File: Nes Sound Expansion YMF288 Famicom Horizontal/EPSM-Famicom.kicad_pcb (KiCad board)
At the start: 4 copper layers, 99 x 91.7 mm, 60 parts, among them J1 CARTRIDGE_F, J2 OUT_1, J3 EPSM_ADDRESSING, J4 CONSOLE_M, J5 AudioJack4_SwitchTR1, U1 74LS174, U10 74LS257, U2 74LS174, U3 74LS139, U4 74LS132, U5 YMF288, U6 BU9480F, U7 74LS257, U8 74LS257, U9 LM358, X1 SG-8002CA

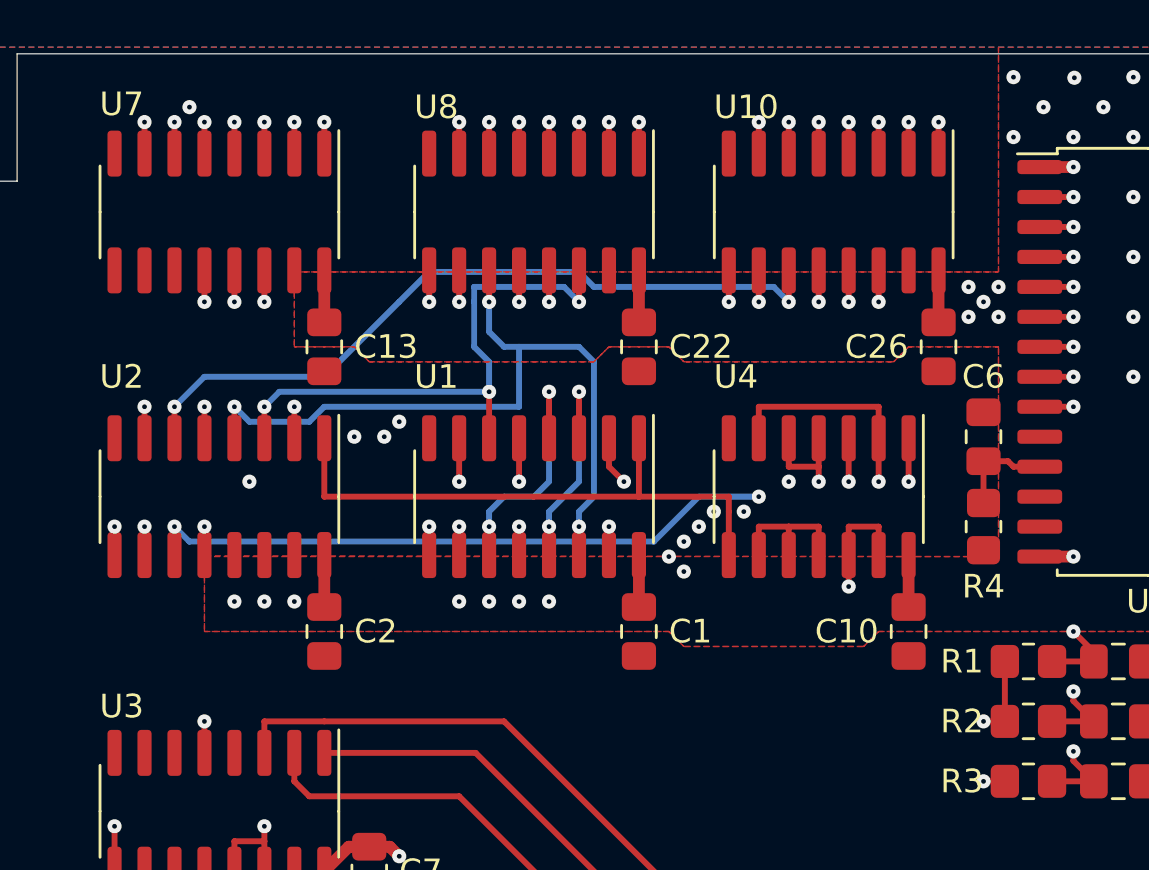
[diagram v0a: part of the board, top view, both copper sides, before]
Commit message: Fix erroneous $4016 data latch lines
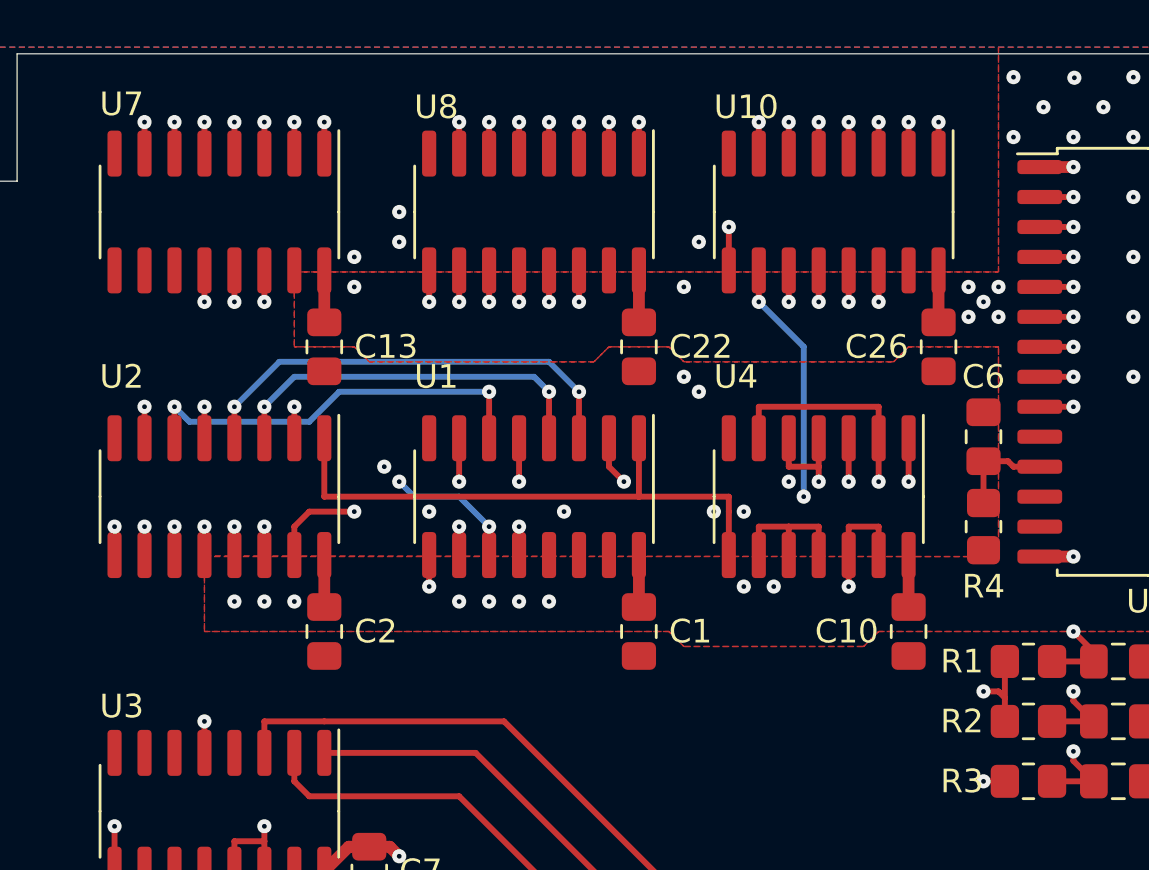
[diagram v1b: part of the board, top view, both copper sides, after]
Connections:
- U1 pad 10: /BUF_D5 -> /BUF_D3
- U1 pad 11: /CPU_D5 -> /CPU_D7
- U1 pad 12: /BUF_D4 -> /$4016_EN
- U1 pad 13: /CPU_D4 -> /VCC
- U1 pad 14: /CPU_D7 -> unconnected-(U1-Pad14)
- U1 pad 15: /BUF_D3 -> unconnected-(U1-Pad15)
- U2 pad 10: /BUF_A1 -> /BUF_D7
- U2 pad 11: /CPU_D2 -> /CPU_D7
- U2 pad 12: /$4016_EN -> /BUF_A0
- U2 pad 13: /VCC -> /CPU_D3
- U2 pad 14: /VCC -> /CPU_D2
- U2 pad 15: unconnected-(U2-Pad15) -> /BUF_A1
- U2 pad 2: /BUF_D6 -> /BUF_D5
- U2 pad 3: /CPU_D6 -> /CPU_D5
- U2 pad 4: /CPU_D7 -> /CPU_D4
- U2 pad 5: /BUF_D7 -> /BUF_D4
- U2 pad 6: /CPU_D3 -> /CPU_D6
- U2 pad 7: /BUF_A0 -> /BUF_D6
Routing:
- net /BUF_D6: track 15.8 -> 31.4 mm
- net /BUF_D3: track 16.9 -> 27.2 mm
- net /CPU_D4: track 104.8 -> 113.2 mm, vias 4 -> 5
- net /BUF_A0: track 27.0 -> 35.0 mm, vias 3 -> 4
- net /CPU_D6: track 104.3 -> 110.7 mm
- net /$4016_EN: track 86.2 -> 80.1 mm, vias 6 -> 5
- net /BUF_CS: track 37.0 -> 31.1 mm, vias 3 -> 2
- net /CPU_D3: track 110.5 -> 104.7 mm, vias 2 -> 3
- net /BUF_A1: track 20.2 -> 25.4 mm, vias 2 -> 3
- net /BUF_D7: track 17.8 -> 22.1 mm
- net /YM_D3: track 19.2 -> 22.9 mm
- net /BUF_D5: track 22.8 -> 19.3 mm
- net /BUF_D4: track 29.9 -> 26.7 mm, vias 3 -> 2
- net /CPU_D7: track 102.4 -> 99.1 mm, vias 3 -> 4
- net /CPU_D2: track 108.3 -> 105.1 mm
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
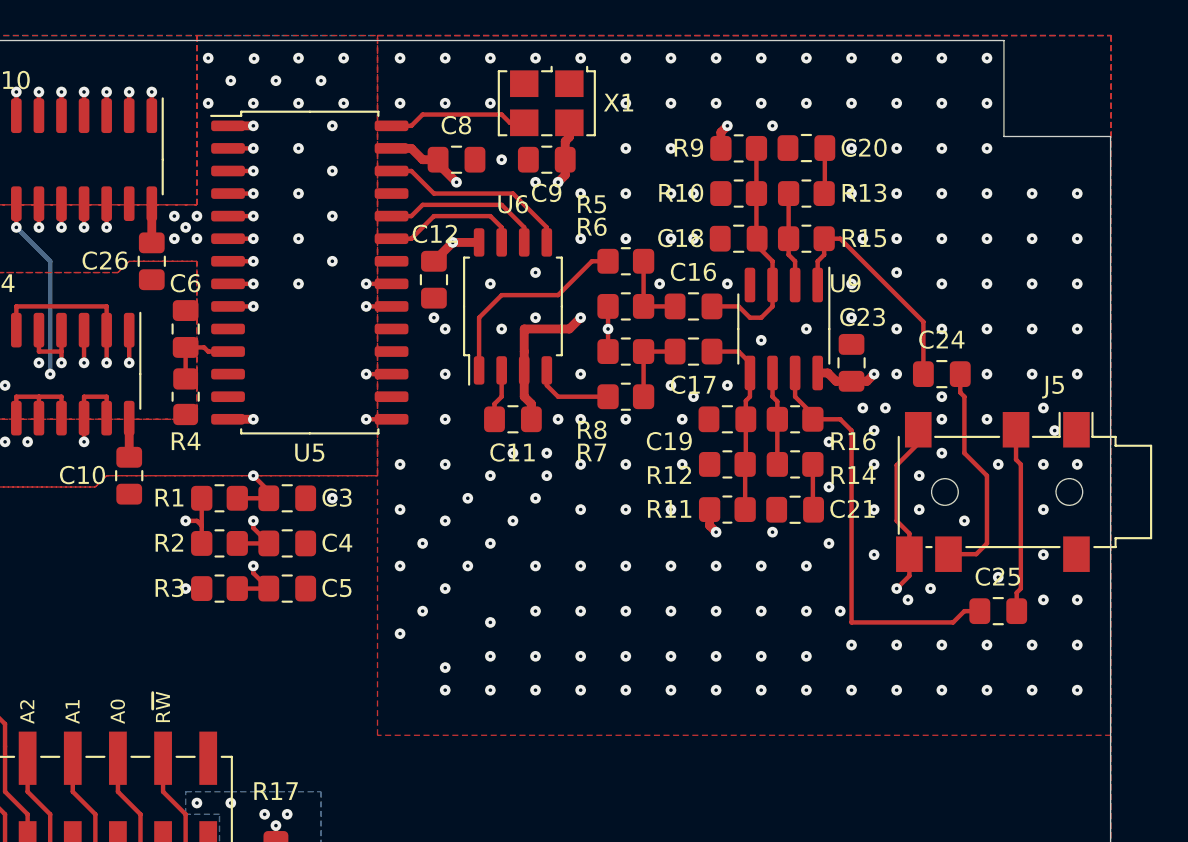
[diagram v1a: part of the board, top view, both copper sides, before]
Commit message: Fix footprint size errors
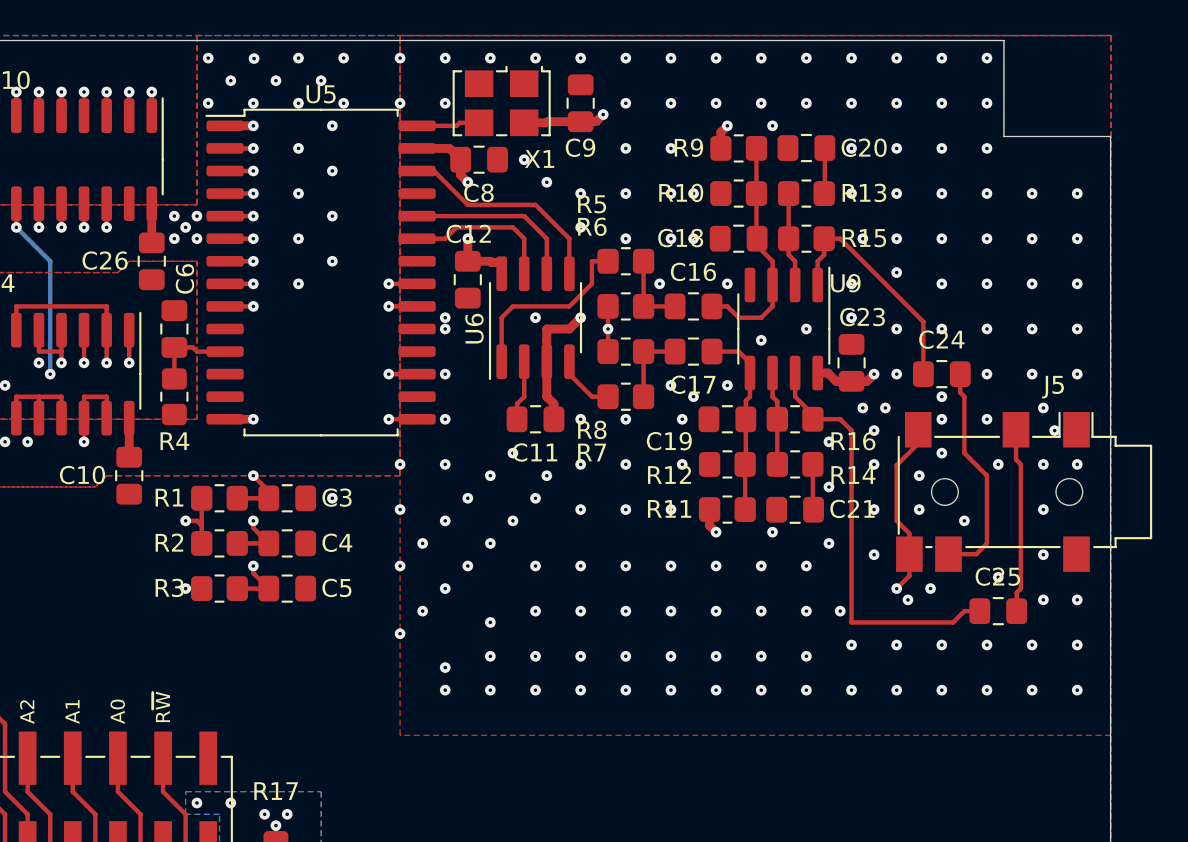
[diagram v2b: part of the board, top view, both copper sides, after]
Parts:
- U1, U2: value 74LS174 -> 74HC174
- U10, U7, U8: value 74LS257 -> 74HC257
- U3: value 74LS139 -> 74HC139
- U4: value 74LS132 -> 74HC132
- U5: footprint EPSM-Famicom:SOP-28_7.5x12.8mm_P1.27mm -> EPSM-Famicom:SOP-28_8.4x18.1mm_P1.27mm
- U6: footprint Package_SO:SOIC-8_5.275x5.275mm_P1.27mm -> Package_SO:SOIC-8_3.9x4.9mm_P1.27mm
- moved C9 3.70 mm to (146.7, 49.5), turned to 90 degrees
- moved X1 2.54 mm to (142.2, 49.5)
- moved C12 1.91 mm to (140.3, 59.5)
- moved U6 1.42 mm to (144.1, 61.6)
- moved C11 1.27 mm to (144.1, 67.3)
- moved C8 1.27 mm to (141.0, 52.7)
- moved U5 0.64 mm to (132.1, 59.1)
- moved C6 0.63 mm to (123.8, 62.2)
- moved R4 0.63 mm to (123.8, 66.0)
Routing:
- net Net-(U5-Pad28): track 7.92 -> 3.56 mm
- net Net-(U5-Pad26): track 10.9 -> 12.9 mm
- net Net-(R5-Pad2): track 11.5 -> 9.88 mm
- net /VCC: track 37.1 -> 38.7 mm
- net Net-(U5-Pad23): track 7.83 -> 9.33 mm
- net Net-(U5-Pad24): track 9.10 -> 10.6 mm
- net /YM_CS: track 49.9 -> 51.2 mm
- net /YM_A1: track 52.2 -> 53.5 mm
- net /YM_A0: track 54.5 -> 55.8 mm
- net /GND: track 52.2 -> 50.9 mm, vias 244 -> 237
- net /AUD_RF: track 57.9 -> 57.2 mm
- net /~{IRQ}: track 71.9 -> 72.4 mm
- net Net-(R7-Pad2): track 4.55 -> 4.04 mm

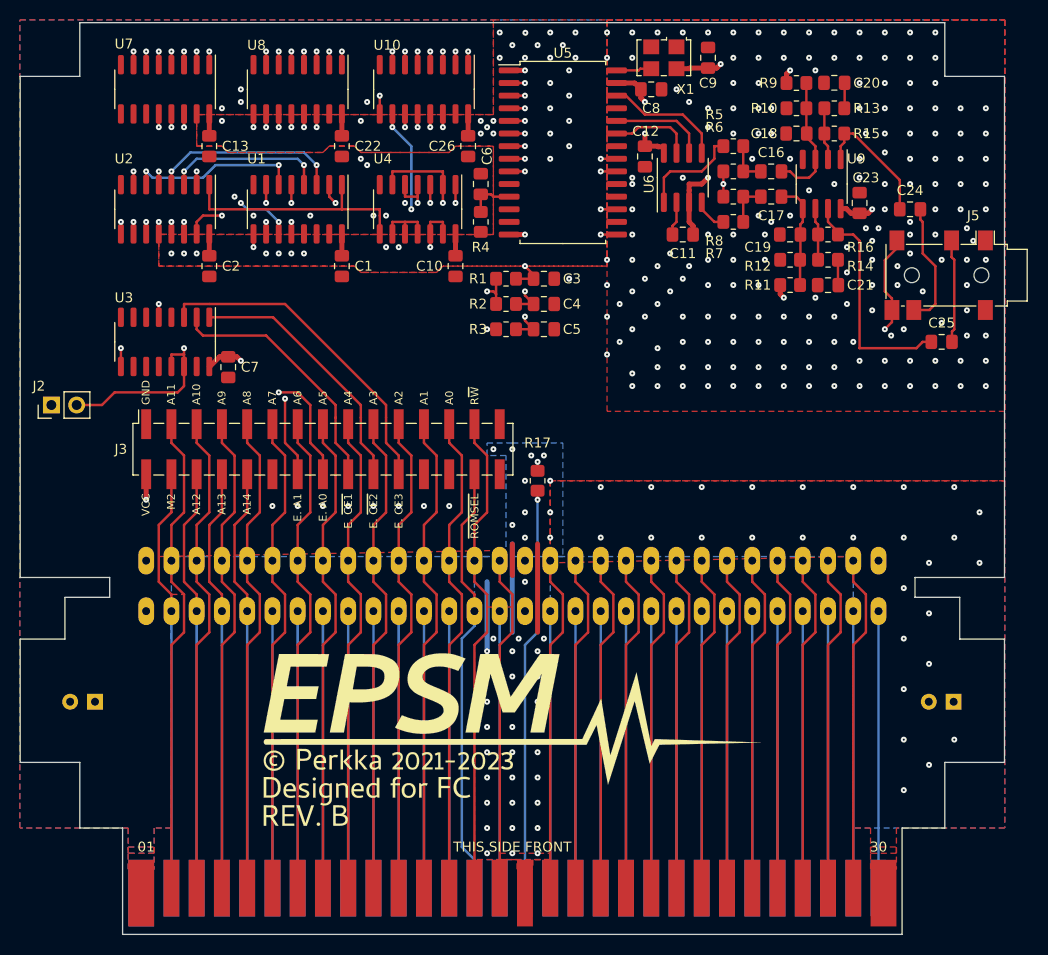
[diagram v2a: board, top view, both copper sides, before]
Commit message: Remove daughterboard connector; use two layers
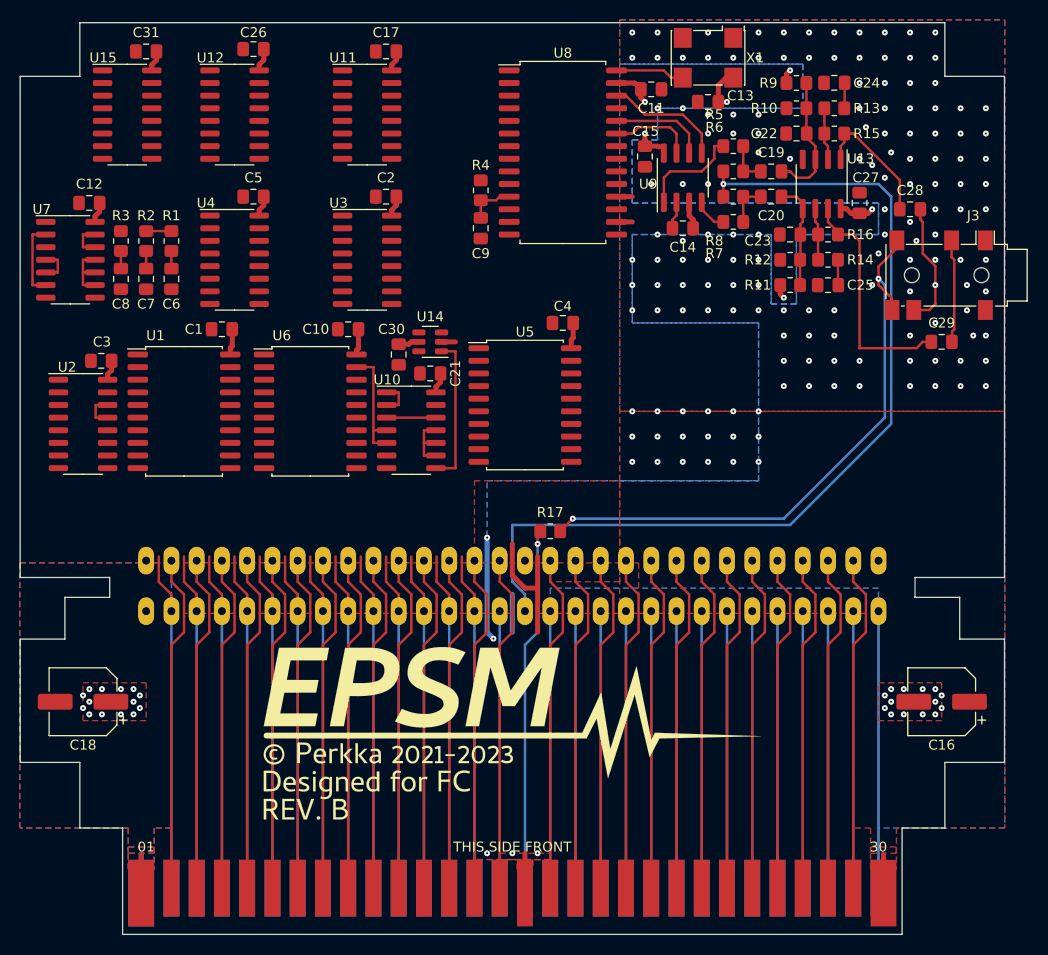
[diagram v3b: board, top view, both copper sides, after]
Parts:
- removed the C14 at (85.0, 114.3)
- removed the C15 at (171.4, 114.3)
- removed the J2 at (80.6, 84.5)
- removed the J3 at (108.0, 88.9)
- added C1: 0.1uF, Capacitor_SMD:C_0805_2012Metric_Pad1.18x1.45mm_HandSolder, F.Cu at (97.8, 76.8)
- added C10: 0.1uF, Capacitor_SMD:C_0805_2012Metric_Pad1.18x1.45mm_HandSolder, F.Cu at (110.5, 76.8)
- added C16: 100uF, Capacitor_SMD:CP_Elec_6.3x5.4, F.Cu at (170.2, 114.3)
- added C18: 100uF, Capacitor_SMD:CP_Elec_6.3x5.4, F.Cu at (83.8, 114.3)
- added C21: 0.1uF, Capacitor_SMD:C_0805_2012Metric_Pad1.18x1.45mm_HandSolder, F.Cu at (118.7, 81.3)
- added C30: 0.1uF, Capacitor_SMD:C_0805_2012Metric_Pad1.18x1.45mm_HandSolder, F.Cu at (115.6, 79.4)
- added C4: 0.1uF, Capacitor_SMD:C_0805_2012Metric_Pad1.18x1.45mm_HandSolder, F.Cu at (132.1, 76.2)
- added U1: 74HC688, Package_SO:SOIC-20W_7.5x12.8mm_P1.27mm, F.Cu at (94.0, 85.1)
- added U10: 74HC132, Package_SO:SOIC-14_3.9x8.7mm_P1.27mm, F.Cu at (116.8, 87.0)
- added U14: 74LVC1G373, Package_TO_SOT_SMD:SOT-23-6, F.Cu at (118.7, 78.1)
- added U5: 74HC688, Package_SO:SOIC-20W_7.5x12.8mm_P1.27mm, F.Cu at (128.3, 84.5)
- added U6: 74HC688, Package_SO:SOIC-20W_7.5x12.8mm_P1.27mm, F.Cu at (106.7, 85.1)
- X1: footprint Oscillator:Oscillator_SMD_SeikoEpson_SG8002LB-4Pin_5.0x3.2mm -> Oscillator:Oscillator_SMD_Abracon_ASV-4Pin_7.0x5.1mm
- moved C8 42.8 mm to (87.6, 71.8), turned to -90 degrees
- moved C7 40.1 mm to (90.2, 71.8), turned to -90 degrees
- moved R3 39.7 mm to (87.6, 68.0), turned to -90 degrees
- moved C6 37.5 mm to (92.7, 71.8), turned to -90 degrees
- moved C12 37.4 mm to (84.5, 64.1), turned to 0 degrees
- moved R2 36.7 mm to (90.2, 68.0), turned to -90 degrees
- moved U7 35.3 mm to (82.5, 69.8), turned to 0 degrees
- moved R1 33.9 mm to (92.7, 68.0), turned to -90 degrees
- moved C26 13.2 mm to (101.0, 48.7), turned to 0 degrees
- moved C3 12.8 mm to (85.7, 80.0), turned to 0 degrees
- moved C17 12.6 mm to (114.3, 48.9), turned to 0 degrees
- moved U2 11.7 mm to (83.8, 86.4), turned to 0 degrees
- moved C31 11.4 mm to (90.2, 48.9), turned to 0 degrees
- moved U3 8.64 mm to (112.4, 69.8), turned to 0 degrees
- moved U4 8.64 mm to (99.1, 69.8), turned to 0 degrees
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- renumbered C8 to C11, C10 to C12, C9 to C13, C11 to C14, C12 to C15, C26 to C17, C16 to C19, C1 to C2, C17 to C20, C18 to C22, C19 to C23, C20 to C24, C21 to C25, C22 to C26, C23 to C27, C24 to C28, C25 to C29, C7 to C3, C13 to C31, C2 to C5, C3 to C6, C4 to C7, C5 to C8, C6 to C9, J4 to J2, J5 to J3, U10 to U11, U8 to U12, U9 to U13, U7 to U15, U3 to U2, U1 to U3, U2 to U4, U4 to U7, U5 to U8, U6 to U9
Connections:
- C11 pad 1: /GND -> GND
- C11 pad 2: /VCC -> VCC
- C12 pad 1: /GND -> GND
- C12 pad 2: /VCC -> VCC
- C13 pad 1: /VCC -> VCC
- C13 pad 2: /GND -> GND
- C14 pad 2: /GND -> GND
- C15 pad 1: /GND -> GND
- C15 pad 2: /VCC -> VCC
- C17 pad 1: /GND -> GND
- C17 pad 2: /VCC -> VCC
- C2 pad 1: /GND -> GND
- C2 pad 2: /VCC -> VCC
- C22 pad 2: /GND -> GND
- C23 pad 2: /GND -> GND
- C24 pad 1: /GND -> GND
- C25 pad 1: /GND -> GND
- C26 pad 1: /GND -> GND
- C26 pad 2: /VCC -> VCC
- C27 pad 1: /GND -> GND
- C27 pad 2: /VCC -> VCC
- C3 pad 1: /GND -> GND
- C3 pad 2: /VCC -> VCC
- C31 pad 1: /GND -> GND
- C31 pad 2: /VCC -> VCC
- C5 pad 1: /GND -> GND
- C5 pad 2: /VCC -> VCC
- C6 pad 2: /GND -> GND
- C7 pad 2: /GND -> GND
- C8 pad 1: Net-(C5-Pad1) -> Net-(C8-Pad1)
- C8 pad 2: /GND -> GND
- C9 pad 1: /GND -> GND
- J1 pad 1: /GND -> GND
- J1 pad 16: /GND -> GND
- J1 pad 30: /VCC -> VCC
- J1 pad 31: /VCC -> VCC
- J2 pad 1: /GND -> GND
- J2 pad 16: /GND -> GND
- J2 pad 30: /VCC -> VCC
- J2 pad 31: /VCC -> VCC
- J3 pad S: /GND -> GND
- R10 pad 2: /GND -> GND
- R11 pad 1: /VCC -> VCC
- R12 pad 2: /GND -> GND
- R3 pad 2: Net-(C5-Pad1) -> Net-(C8-Pad1)
- R4 pad 1: /VCC -> VCC
- R9 pad 1: /VCC -> VCC
- U11 pad 12: /YM_D2 -> /YM_D1
- U11 pad 13: /BUF_D2 -> /BUF_D1
- U11 pad 14: /CPU_D2 -> /CPU_D1
- U11 pad 15: /GND -> GND
- U11 pad 16: /VCC -> VCC
- U11 pad 5: /CPU_D1 -> /CPU_D2
- U11 pad 6: /BUF_D1 -> /BUF_D2
- U11 pad 7: /YM_D1 -> /YM_D2
- U11 pad 8: /GND -> GND
- U12 pad 12: /YM_D6 -> /YM_D5
- U12 pad 13: /BUF_D6 -> /BUF_D5
- U12 pad 14: /CPU_D6 -> /CPU_D5
- U12 pad 15: /GND -> GND
- U12 pad 16: /VCC -> VCC
- U12 pad 5: /CPU_D5 -> /CPU_D6
- U12 pad 6: /BUF_D5 -> /BUF_D6
- U12 pad 7: /YM_D5 -> /YM_D6
- U12 pad 8: /GND -> GND
- U13 pad 4: /GND -> GND
- U13 pad 8: /VCC -> VCC
- U15 pad 10: /GND -> GND
- U15 pad 11: /GND -> GND
- U15 pad 12: /YM_CS -> /YM_A0
- U15 pad 13: /~{CS} -> /BUF_A1
- U15 pad 14: /BUF_CS -> /EPSM_A0
- U15 pad 15: /GND -> GND
- U15 pad 16: /VCC -> VCC
- U15 pad 5: /EPSM_A0 -> /BUF_CS
- U15 pad 6: /BUF_A1 -> /~{CS}
- U15 pad 7: /YM_A0 -> /YM_CS
- U15 pad 8: /GND -> GND
- U2 pad 1: /EPSM_~{CE2} -> /$401x_~{CE}
- U2 pad 15: /GND -> GND
- U2 pad 16: /VCC -> VCC
- U2 pad 2: /EPSM_~{CE1} -> GND
- U2 pad 3: /EPSM_CE3 -> VCC
- U2 pad 8: /GND -> GND
- U3 pad 10: /BUF_D3 -> unconnected-(U3-Pad10)
- U3 pad 11: /CPU_D7 -> VCC
- U3 pad 12: /$4016_EN -> /BUF_D1
- U3 pad 13: /VCC -> /CPU_D5
- U3 pad 14: unconnected-(U1-Pad14) -> /CPU_D7
- U3 pad 15: unconnected-(U1-Pad15) -> /BUF_D3
- U3 pad 16: /VCC -> VCC
- U3 pad 2: /BUF_D0 -> /BUF_D2
- U3 pad 3: /CPU_D4 -> /CPU_D6
- U3 pad 4: /CPU_D5 -> /CPU_D4
- U3 pad 5: /BUF_D1 -> /BUF_D0
- U3 pad 6: /CPU_D6 -> VCC
- U3 pad 7: /BUF_D2 -> /$4016_EN
- U3 pad 8: /GND -> GND
- U4 pad 10: /BUF_D7 -> /BUF_A1
- U4 pad 11: /CPU_D7 -> /CPU_D2
- U4 pad 12: /BUF_A0 -> /BUF_D5
- U4 pad 13: /CPU_D3 -> /CPU_D5
- U4 pad 14: /CPU_D2 -> /CPU_D7
- U4 pad 15: /BUF_A1 -> /BUF_D7
- U4 pad 16: /VCC -> VCC
- U4 pad 2: /BUF_D5 -> /BUF_D6
- U4 pad 3: /CPU_D5 -> /CPU_D6
- U4 pad 6: /CPU_D6 -> /CPU_D3
- U4 pad 7: /BUF_D6 -> /BUF_A0
- U4 pad 8: /GND -> GND
- U7 pad 12: Net-(C5-Pad1) -> Net-(U7-Pad12)
- U7 pad 13: Net-(C5-Pad1) -> Net-(U7-Pad12)
- U7 pad 14: /VCC -> VCC
- U7 pad 7: /GND -> GND
- U8 pad 1: /GND -> GND
- U8 pad 12: /VCC -> VCC
- U8 pad 14: /GND -> GND
- U8 pad 16: /GND -> GND
- U8 pad 18: /GND -> GND
- U8 pad 19: /VCC -> VCC
- U8 pad 22: /VCC -> VCC
- U8 pad 27: /VCC -> VCC
- U9 pad 3: /GND -> GND
- U9 pad 8: /VCC -> VCC
- X1 pad 2: /GND -> GND
- X1 pad 4: /VCC -> VCC
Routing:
- net /CPU_D4: track 113.2 -> 33.9 mm, vias 5 -> 0
- net /CPU_D5: track 113.2 -> 33.9 mm, vias 5 -> 0
- net /$4016_EN: track 80.1 -> 2.54 mm, vias 5 -> 0
- net /CPU_D6: track 110.7 -> 33.9 mm, vias 3 -> 0
- net /CPU_D2: track 105.1 -> 33.9 mm, vias 3 -> 0
- net /CPU_D3: track 104.7 -> 33.9 mm, vias 3 -> 0
- net /CPU_D7: track 99.1 -> 33.9 mm, vias 4 -> 0
- net /CPU_D1: track 90.5 -> 33.9 mm, vias 1 -> 0
- net /YM_A0: track 55.8 -> 0.00 mm, vias 2 -> 0
- net VCC: track 0.00 -> 53.6 mm, vias 0 -> 38
- net /YM_A1: track 53.5 -> 0.00 mm, vias 2 -> 0
- net /CPU_D0: track 87.3 -> 33.9 mm, vias 1 -> 0
- net /EPSM_A0: track 52.7 -> 0.00 mm, vias 3 -> 0
- net /YM_CS: track 51.2 -> 0.00 mm, vias 2 -> 0
- net /GND: track 50.9 -> 0.00 mm, vias 237 -> 0
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- added copper zone on B.Cu, net GND
- added copper zone on F.Cu, net GND
- added copper zone on B.Cu, net VCC
- added copper zone on F.Cu, net VCC
- removed copper zone on B.Cu, net /GND
- removed copper zone on F.Cu, net /GND
- removed copper zone on In1.Cu, net /GND
- removed copper zone on In2.Cu, net /GND
- removed copper zone on B.Cu, net /VCC
- removed copper zone on F.Cu, net /VCC
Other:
- copper layers 4 -> 2
- board text removed: "GND A11 A10 A9 A8 A7 A6 A5 A4 A3 A2 A1 A0 R~{W}"
- board text removed: "VCC M2 A12 A13 A14 E. A1 E. A0 E. ~{CE1} E. ~{CE2} E. CE3 ~{ROMSEL}"
